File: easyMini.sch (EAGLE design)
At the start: 30 parts

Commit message: Visual adjustments
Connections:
- removed net N$14: U$2.CSB@5
- new net N$16: U$1.PA12, U$2.CSB@5
- new net N$9: U$1.PA10, U$5.CS#
- net N$15: now also U$1.PA11
- net N$20: now also U$1.PB1
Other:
- moved on the sheet: C1, C13, C2, C3, C4, C5, C8, LED1, LED2, LED3, LED4, R1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

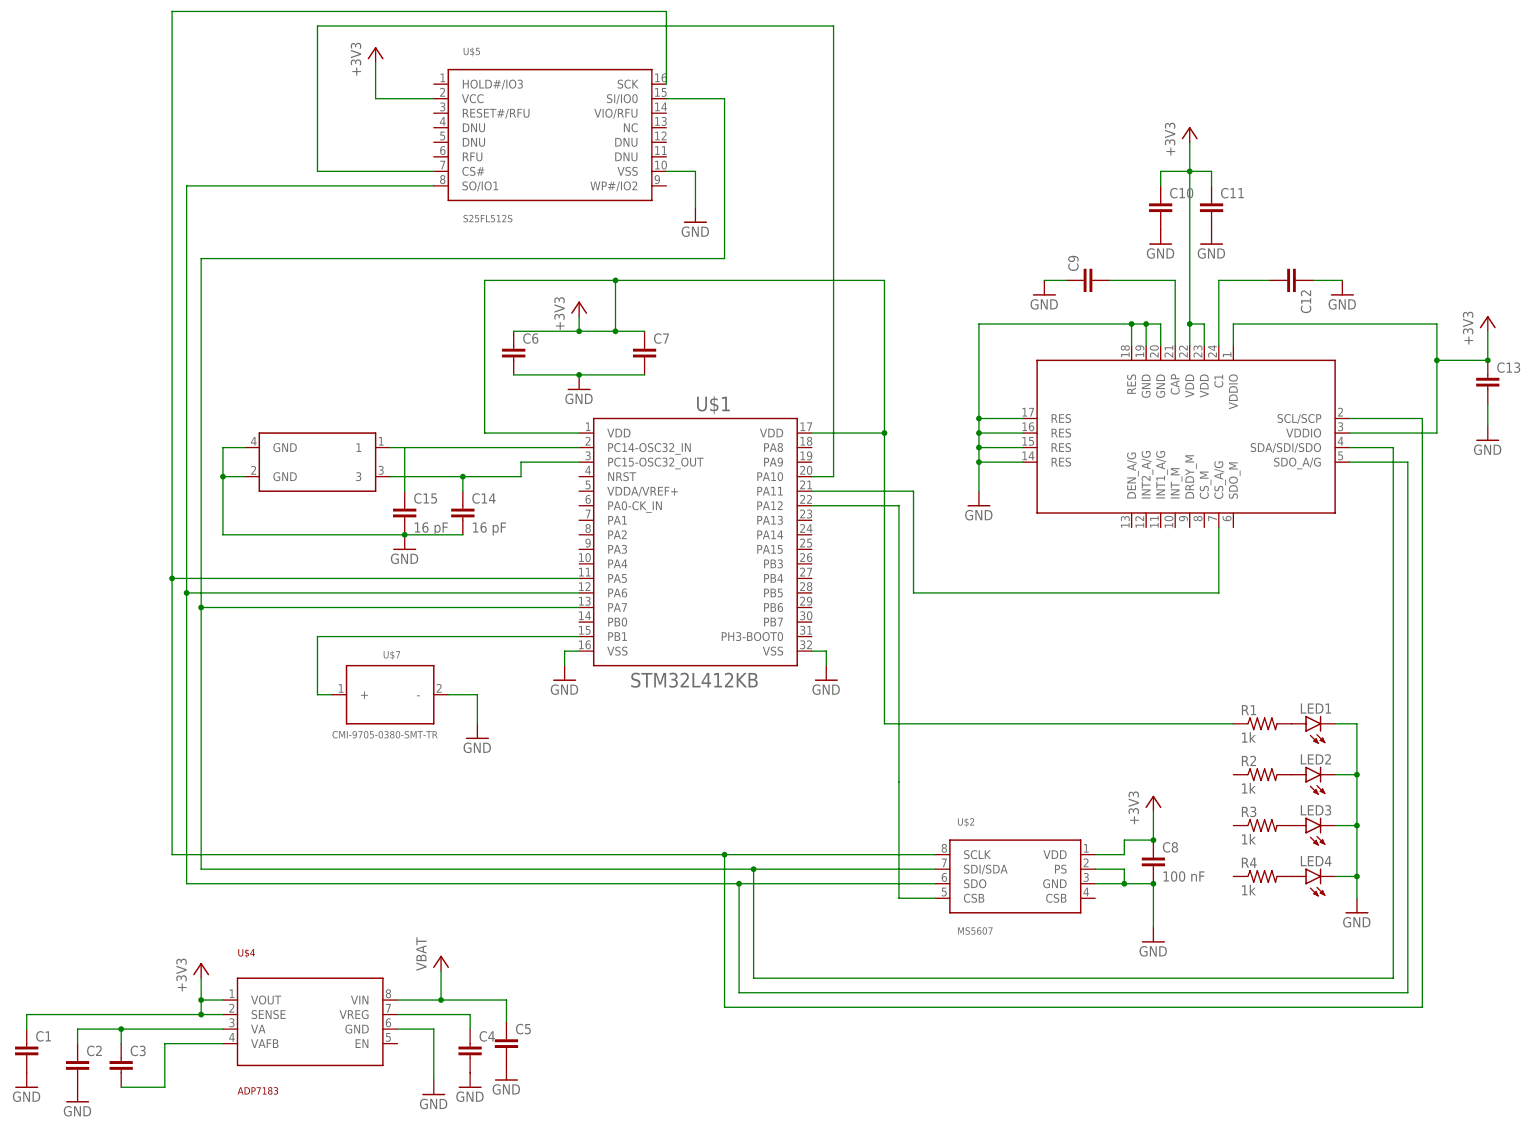
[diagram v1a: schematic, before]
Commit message: Added board design
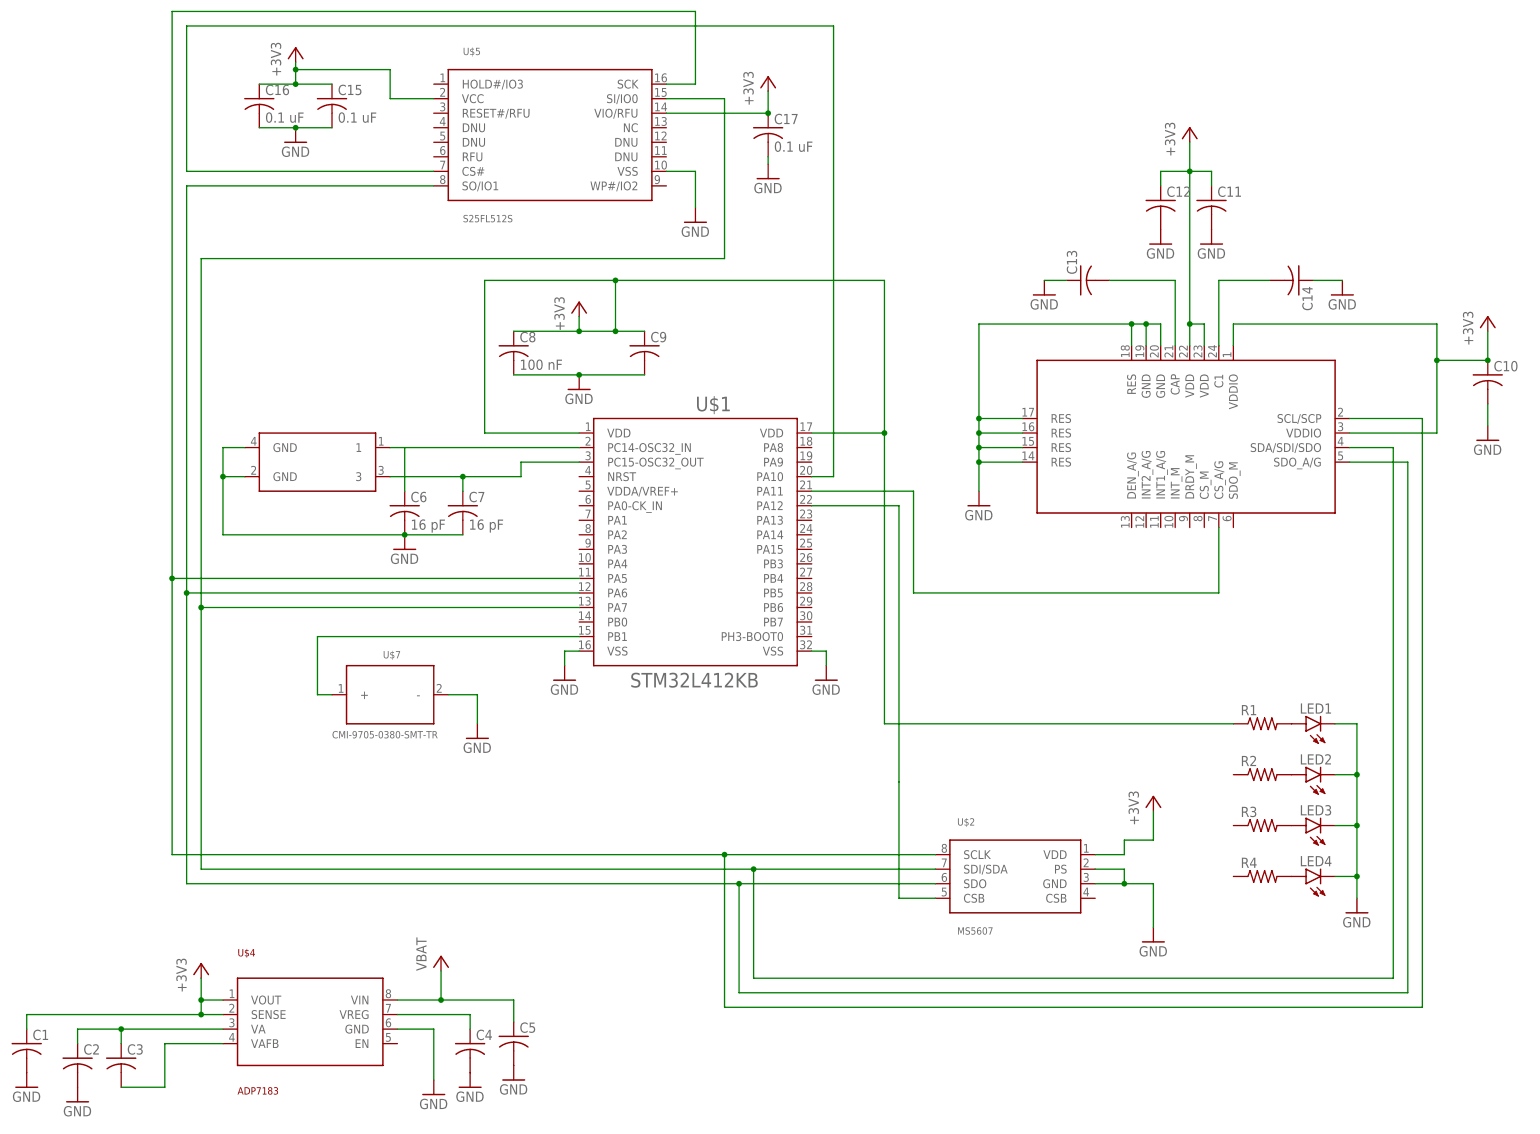
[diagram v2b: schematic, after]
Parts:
- added C16, C17: 0.1 uF, rcl:C-USC0805
- C1, C10, C11, C12, C13, C2, C3, C4, C5, C8, C9: device rcl:C-EU025-025X050 -> rcl:C-USC0805
- C14: value 16 pF -> (none); device rcl:C-EU025-025X050 -> rcl:C-USC0805
- C15: value 16 pF -> 0.1 uF; device rcl:C-EU025-025X050 -> rcl:C-USC0805
- C6, C7: value (none) -> 16 pF; device rcl:C-EU025-025X050 -> rcl:C-USC0805
- R1, R2, R3, R4: value 1k -> (none); device rcl:R-US_0204/7 -> rcl:R-US_M0805
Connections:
- net +3V3: now also C12.1, C15.1, C16.1, C17.1, C9.1, U$5.VIO/RFU; no longer C13.1, C6.1, C7.1
- net GND: now also C12.2, C13.1, C14.1, C16.2, C17.2, C9.2; no longer C12.1, C13.2, C14.2, C9.1
- net N$24: now also C6.1; no longer C15.1
- net N$25: now also C7.1; no longer C14.1
- net N$4: now also C13.2; no longer C9.2
- net N$5: now also C14.2; no longer C12.2
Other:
- moved on the sheet: C10, C12, C13, C14, C15, C5, C6, C7, C8, C9

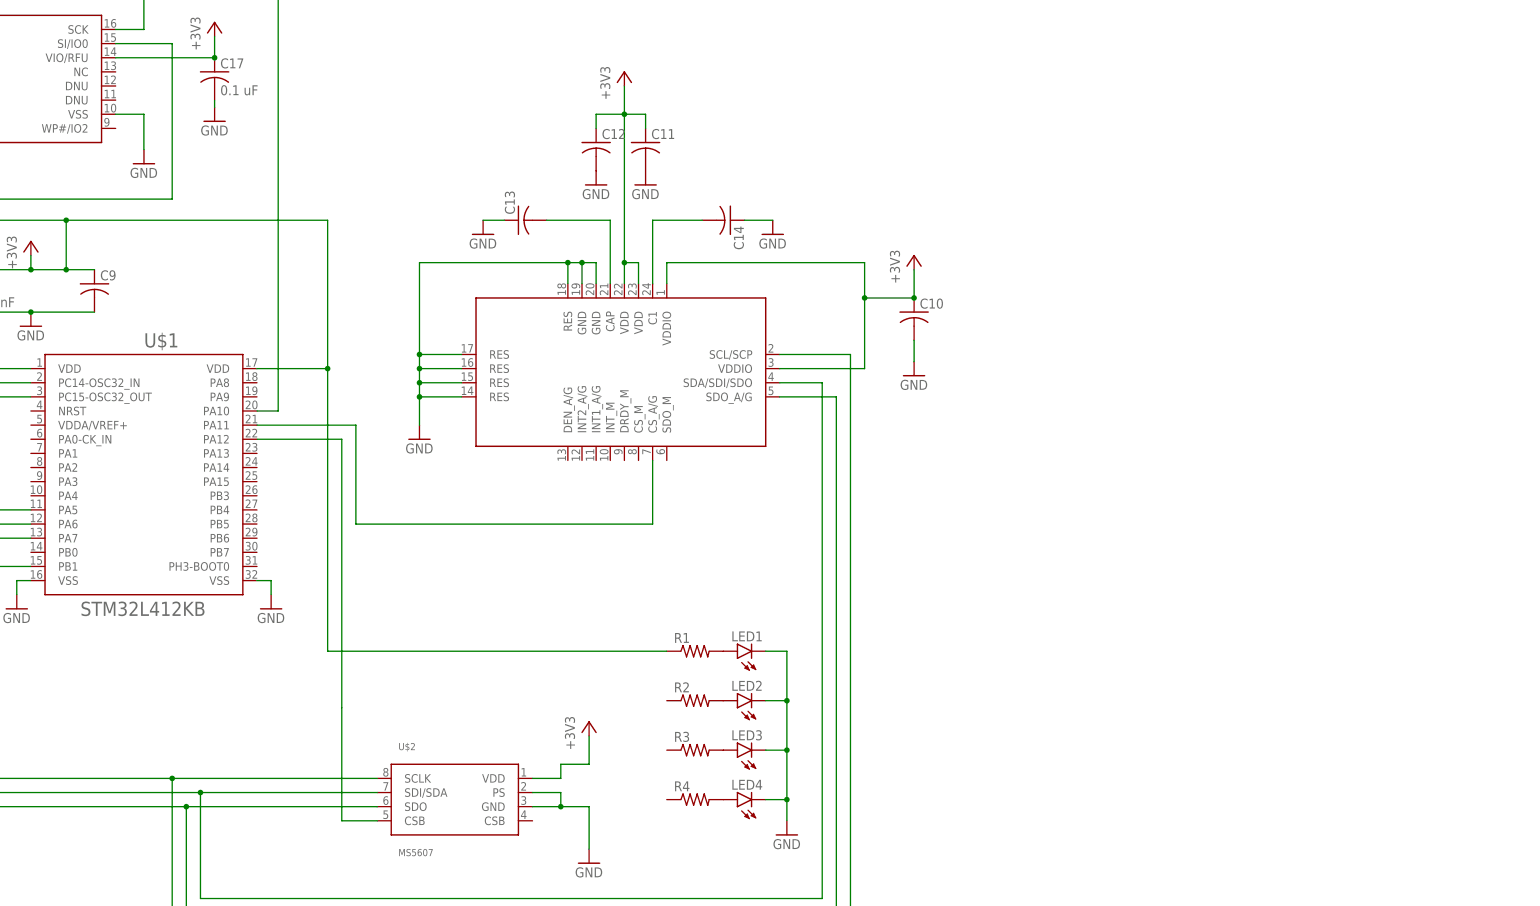
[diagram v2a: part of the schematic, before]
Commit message: Added pyro fets, resistors, and connectors. Modified board design to make more compact.
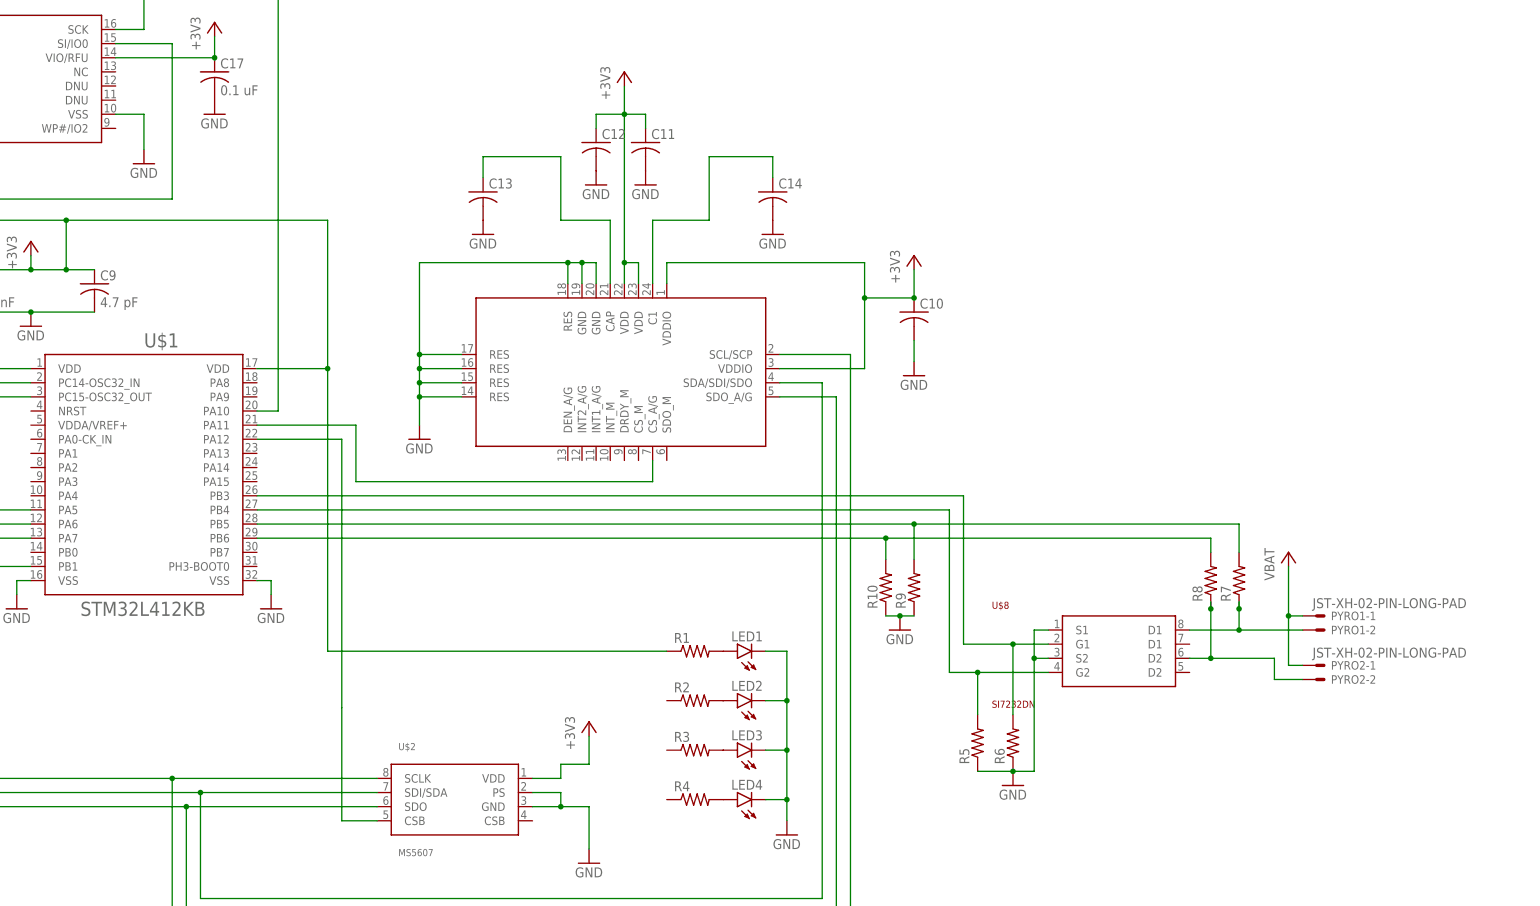
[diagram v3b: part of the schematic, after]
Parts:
- added PYRO1, PYRO2: JST-XH-02-PIN-LONG-PAD, Rembrandt Electronics - JST XH Connectors v1-0:JST-XH-02-PIN-LONG-PAD
- added R10, R5, R6, R7, R8, R9: (no value), rcl:R-US_M0805
- added U$8: SI7232DN, generalUse:SI7232DN
- C9: value (none) -> 4.7 pF
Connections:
- new net N$14: PYRO1-2.S, R7.1, U$8.D1@8
- new net N$17: PYRO2-2.S, R8.1, U$8.D2@6
- new net N$18: R6.2, U$1.PB3, U$8.G1
- new net N$19: R5.2, U$1.PB4, U$8.G2
- new net N$21: R7.2, R9.2, U$1.PB5
- new net N$22: R10.2, R8.2, U$1.PB6
- net +3V3: now also PYRO1-1.S, PYRO2-1.S
- net GND: now also C13.2, C14.2, R10.1, R5.1, R6.1, R9.1, U$8.S1, U$8.S2; no longer C13.1, C14.1
- net N$4: now also C13.1; no longer C13.2
- net N$5: now also C14.1; no longer C14.2
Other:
- moved on the sheet: C13, C14
